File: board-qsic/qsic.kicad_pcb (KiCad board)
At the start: 4 copper layers, 214.1 x 131.7 mm, 173 parts, among them J101 Conn_02x05_Odd_Even, J102 Conn_02x07_Odd_Even, J301 SD Card, J302 SD Card, J501 USB_A, J601 QBUS_A, J602 QBUS_B, P501 Indicator Panel, U101 XC7A75T-CSG324, U1304 TPS82085, U1305 TPS82085, U1306 TPS82085, U1307 TPS82085, U301 IS43TR16128B, U501 MT25Q-mlq8, U502 TPS2561, U503 MAX3033E, U504 USB3340, U601 DS8641-small, U602 DS8641-small, U603 DS8641-small, U604 DS8641-small, U605 DS8641-small, U606 DS8641-small, U607 DS8641-small, U608 DS8641-small, U609 DS8641-small, U610 DS8641-small, U611 DS8641-small, U621 74LVC8T245-small, U622 74LVC8T245-small, U623 74LVC8T245-small, U624 74LVC8T245-small, U625 74LVC8T245-small, U626 74LVC8T245-small, U627 74LVC8T245-small, U628 74LVC8T245-small, U629 74LVC8T245-small, U630 74LVC8T245-small, U631 74LVC8T245-small, X501 ASE-24.000MHz

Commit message: Updated the date on all the pages.
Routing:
- net /QBUS & I/O/RPOK: track 55.1 -> 58.3 mm
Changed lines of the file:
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@@
     (thickness 1.6)
     (drawings 38)
-    (tracks 3850)
+    (tracks 3851)
     (zones 0)
     (modules 173)
@@
   (title_block
     (title QSIC)
-    (date 2019-10-10)
+    (date 2019-10-12)
     (rev 0.2)
   )
@@
   )
   (setup
-    (last_trace_width 0.127)
+    (last_trace_width 0.254)
     (user_trace_width 0.127)
     (user_trace_width 0.1524)
@@
     (visible_elements FFFFFF7F)
     (pcbplotparams
-      (layerselection 0x200f0_80000001)
+      (layerselection 0x200f0_ffffffff)
       (usegerberextensions false)
       (usegerberattributes false)
       (usegerberadvancedattributes false)
       (creategerberjobfile false)
-      (excludeedgelayer true)
+      (excludeedgelayer false)
       (linewidth 0.100000)
       (plotframeref false)
@@
   (segment (start 158.876999 94.487999) (end 158.75 94.361) (width 0.127) (layer F.Cu) (net 365))
   (via (at 159.258004 94.234) (size 0.254) (drill 0.2032) (layers F.Cu B.Cu) (net 366))
-  (segment (start 178.518 103.449) (end 168.473004 103.449) (width 0.127) (layer F.Cu) (net 366))
-  (segment (start 168.473004 103.449) (end 159.385003 94.360999) (width 0.127) (layer F.Cu) (net 366))
-  (segment (start 159.385003 94.360999) (end 159.258004 94.234) (width 0.127) (layer F.Cu) (net 366))
   (segment (start 134.01854 89.00146) (end 134.41708 89.4) (width 0.127) (layer F.Cu) (net 366))
   (segment (start 134.546999 89.273001) (end 134.42 89.4) (width 0.127) (layer B.Cu) (net 366))
@@
   (segment (start 156.337004 91.313) (end 139.573 91.313) (width 0.127) (layer B.Cu) (net 366))
   (segment (start 139.573 91.313) (end 137.336915 89.076915) (width 0.127) (layer B.Cu) (net 366))
+  (segment (start 159.385003 94.360999) (end 159.258004 94.234) (width 0.127) (layer F.Cu) (net 366))
+  (segment (start 178.518 103.449) (end 177.516 103.449) (width 0.127) (layer F.Cu) (net 366))
+  (segment (start 168.592506 103.568502) (end 159.385003 94.360999) (width 0.127) (layer F.Cu) (net 366))
+  (segment (start 177.396498 103.568502) (end 168.592506 103.568502) (width 0.127) (layer F.Cu) (net 366))
+  (segment (start 177.516 103.449) (end 177.396498 103.568502) (width 0.127) (layer F.Cu) (net 366))
   (via (at 134.42 86.2) (size 0.254) (drill 0.2032) (layers F.Cu B.Cu) (net 367))
   (segment (start 134.01854 85.80146) (end 134.02146 85.80146) (width 0.127) (layer F.Cu) (net 367) (status 30))
@@
   (segment (start 134.01854 85.00146) (end 134.02146 85.00146) (width 0.127) (layer F.Cu) (net 368) (status 30))
   (via (at 134.42 85.4) (size 0.254) (drill 0.2032) (layers F.Cu B.Cu) (net 368))
-  (via (at 176.82 102.8) (size 0.254) (drill 0.2032) (layers F.Cu B.Cu) (net 368))
-  (segment (start 178.518 102.799) (end 176.821 102.799) (width 0.127) (layer F.Cu) (net 368) (status 10))
-  (segment (start 176.821 102.799) (end 176.82 102.8) (width 0.127) (layer F.Cu) (net 368))
-  (segment (start 164.084 85.471) (end 154.94 85.471) (width 0.127) (layer B.Cu) (net 368))
   (segment (start 134.42 85.4) (end 134.82 85) (width 0.127) (layer Pwr.Cu) (net 368))
   (segment (start 140.282395 85.725) (end 140.462 85.725) (width 0.127) (layer Pwr.Cu) (net 368))
-  (segment (start 154.686 85.725) (end 140.641605 85.725) (width 0.127) (layer B.Cu) (net 368))
-  (segment (start 176.82 102.8) (end 171.958 97.938) (width 0.127) (layer B.Cu) (net 368))
   (segment (start 134.82 85) (end 136.42 85) (width 0.127) (layer Pwr.Cu) (net 368))
   (segment (start 137.145 85.725) (end 140.282395 85.725) (width 0.127) (layer Pwr.Cu) (net 368))
-  (segment (start 154.94 85.471) (end 154.686 85.725) (width 0.127) (layer B.Cu) (net 368))
   (segment (start 136.42 85) (end 137.145 85.725) (width 0.127) (layer Pwr.Cu) (net 368))
-  (segment (start 171.958 93.345) (end 164.084 85.471) (width 0.127) (layer B.Cu) (net 368))
-  (segment (start 171.958 97.938) (end 171.958 93.345) (width 0.127) (layer B.Cu) (net 368))
-  (segment (start 140.641605 85.725) (end 140.462 85.725) (width 0.127) (layer B.Cu) (net 368))
   (via (at 140.462 85.725) (size 0.254) (drill 0.2032) (layers F.Cu B.Cu) (net 368))
+  (segment (start 140.462 85.725) (end 154.686 85.725) (width 0.127) (layer B.Cu) (net 368))
+  (segment (start 171.322998 102.563395) (end 171.322998 102.743) (width 0.127) (layer B.Cu) (net 368))
+  (segment (start 154.94 85.471) (end 164.084 85.471) (width 0.127) (layer B.Cu) (net 368))
+  (segment (start 171.378998 102.799) (end 171.322998 102.743) (width 0.127) (layer F.Cu) (net 368))
+  (segment (start 164.084 85.471) (end 171.322998 92.709998) (width 0.127) (layer B.Cu) (net 368))
+  (segment (start 171.322998 92.709998) (end 171.322998 102.563395) (width 0.127) (layer B.Cu) (net 368))
+  (via (at 171.322998 102.743) (size 0.254) (drill 0.2032) (layers F.Cu B.Cu) (net 368))
+  (segment (start 178.518 102.799) (end 171.378998 102.799) (width 0.127) (layer F.Cu) (net 368))
+  (segment (start 154.686 85.725) (end 154.94 85.471) (width 0.127) (layer B.Cu) (net 368))
   (via (at 134.42 84.6) (size 0.254) (drill 0.2032) (layers F.Cu B.Cu) (net 369))
   (segment (start 134.01854 84.20146) (end 134.02146 84.20146) (width 0.127) (layer F.Cu) (net 369) (status 30))

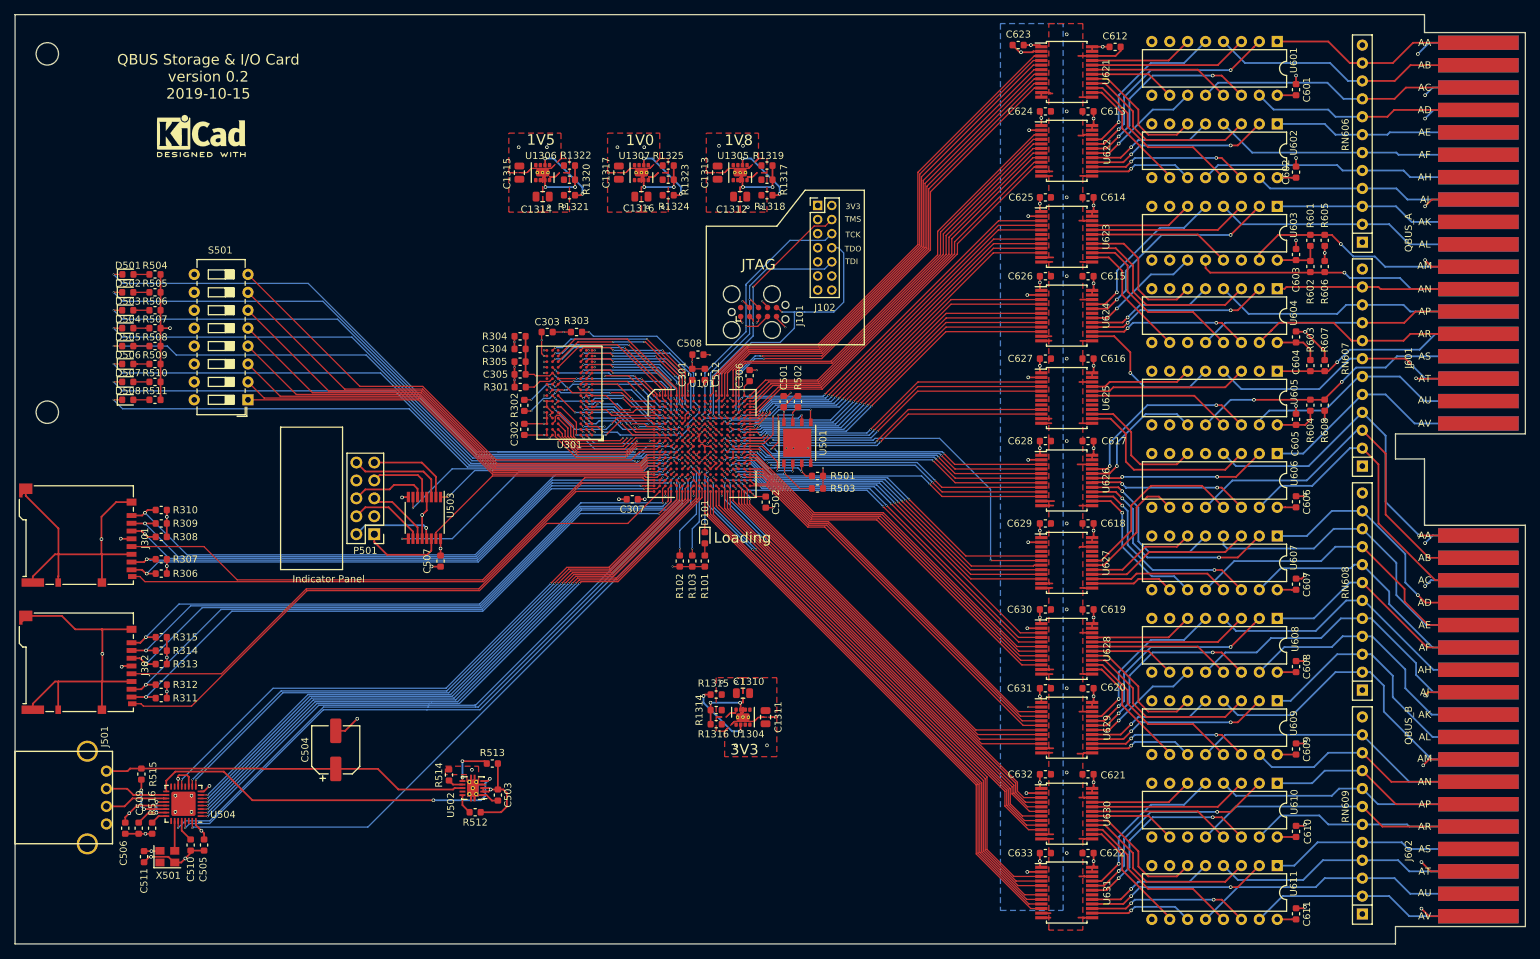
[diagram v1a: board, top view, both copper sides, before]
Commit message: Changes from Emanuel's comments.
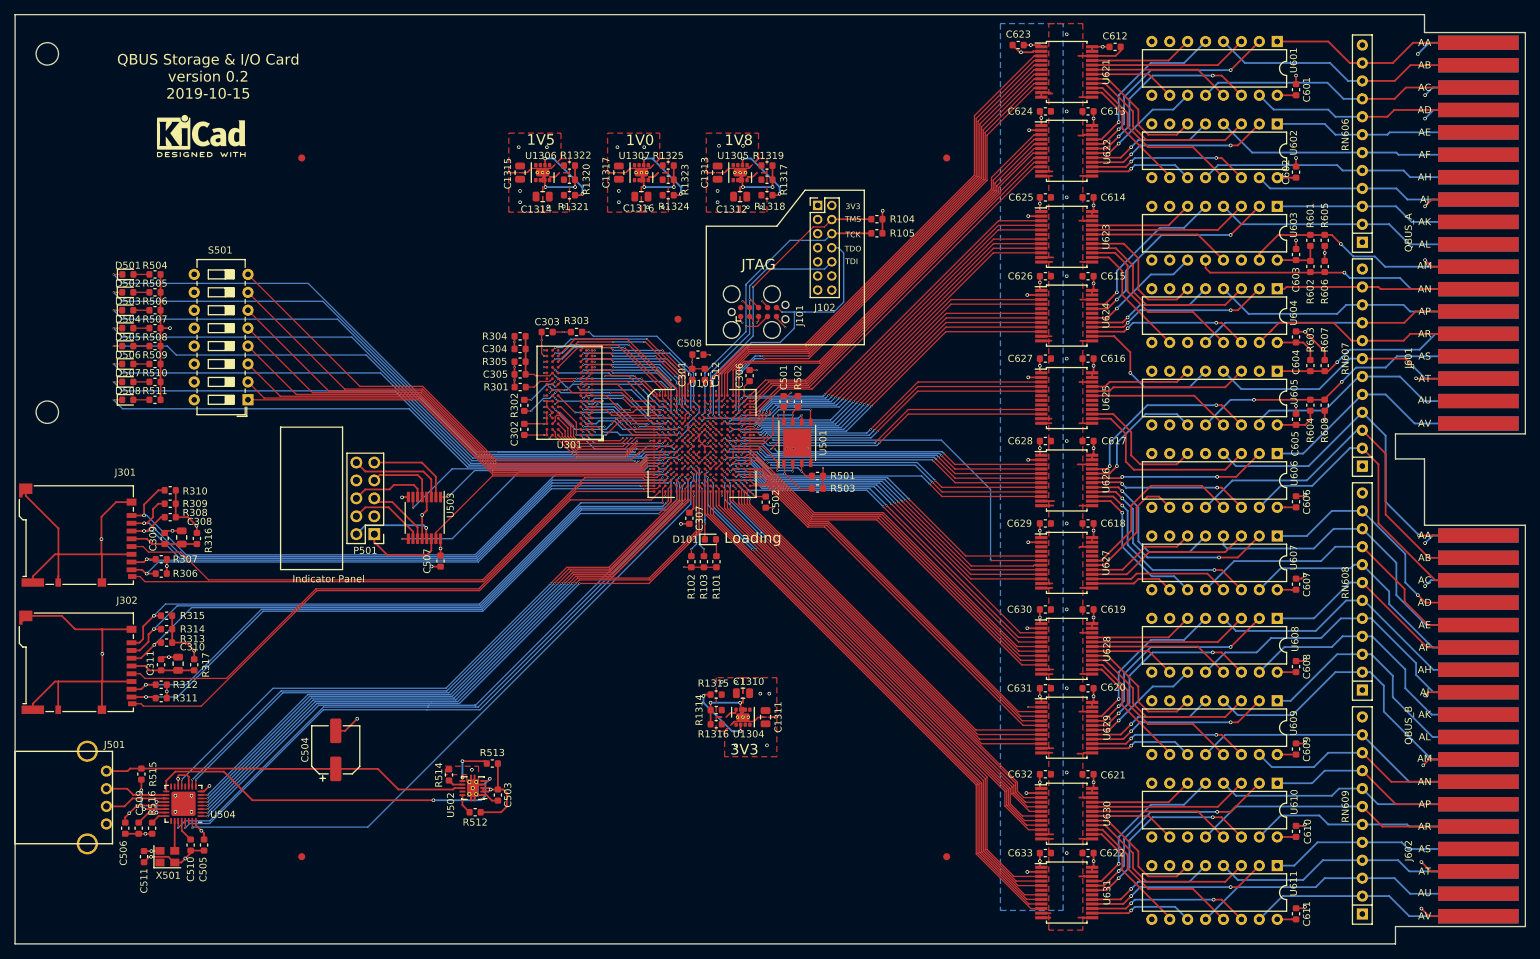
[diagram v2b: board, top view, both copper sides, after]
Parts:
- added C308: 22uF, Capacitor_SMD:C_0805_2012Metric, F.Cu at (56.6, 99.5)
- added C309: 100nF, Capacitor_SMD:C_0603_1608Metric, F.Cu at (54.2, 99.7)
- added C310: 22uF, Capacitor_SMD:C_0805_2012Metric, F.Cu at (56.1, 117.4)
- added C311: 100nF, Capacitor_SMD:C_0603_1608Metric, F.Cu at (53.7, 117.6)
- added FID101: Fiducial, Fiducial:Fiducial_1mm_Mask2mm, F.Cu at (73.7, 45.7)
- added FID102: Fiducial, Fiducial:Fiducial_1mm_Mask2mm, F.Cu at (165.1, 45.7)
- added FID103: Fiducial, Fiducial:Fiducial_1mm_Mask2mm, F.Cu at (73.7, 144.8)
- added FID104: Fiducial, Fiducial:Fiducial_1mm_Mask2mm, F.Cu at (165.1, 144.8)
- added FID105: Fiducial, Fiducial:Fiducial_1mm_Mask2mm, F.Cu at (127.0, 68.6)
- added R104: 10k, Resistor_SMD:R_0603_1608Metric, F.Cu at (155.2, 54.4)
- added R105: 10k, Resistor_SMD:R_0603_1608Metric, F.Cu at (155.2, 56.4)
- added R316: 4.7, Resistor_SMD:R_0603_1608Metric, F.Cu at (58.8, 99.7)
- added R317: 4.7, Resistor_SMD:R_0603_1608Metric, F.Cu at (58.4, 117.6)
- R304, R305: value 47 -> 47 1%
- moved C307 8.53 mm to (128.6, 96.8), turned to 270 degrees
- moved R315 3.14 mm to (54.5, 110.6)
- moved R313 3.14 mm to (54.5, 114.4)
- moved R314 3.14 mm to (54.5, 112.5)
- moved R308 3.07 mm to (55.0, 96.6)
- moved R310 3.07 mm to (55.0, 92.8)
- moved R309 3.07 mm to (55.0, 94.7)
- moved R101 1.65 mm to (132.5, 103.0)
- moved R103 1.65 mm to (130.7, 103.0)
- moved R102 1.65 mm to (128.9, 103.0)
- moved D101 0.83 mm to (131.6, 99.8), turned to 0 degrees
- moved C1315 0.10 mm to (104.6, 47.8)
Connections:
- J301 pad 4: /3V3 -> Net-(C308-Pad1)
- J302 pad 4: /3V3 -> Net-(C310-Pad1)
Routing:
- net /3V3: track 125.3 -> 136.5 mm, vias 56 -> 54
- net Net-(C308-Pad1): track 0.00 -> 9.57 mm
- net Net-(C310-Pad1): track 0.00 -> 9.14 mm
- net /TMS: track 37.3 -> 42.9 mm
- net /TCK: track 40.5 -> 46.1 mm
- net GND: track 382.5 -> 387.7 mm, vias 126 -> 136
- net /QBUS & I/O/sd0_dat2: track 85.8 -> 89.1 mm
- net /QBUS & I/O/sd0_dat3: track 84.8 -> 88.0 mm
- net /QBUS & I/O/usb0_d1: track 91.0 -> 93.8 mm
- net /QBUS & I/O/usb0_d0: track 89.9 -> 92.6 mm
- net /QBUS & I/O/usb0_nxt: track 91.4 -> 94.2 mm
- net /QBUS & I/O/sd0_cmd: track 84.4 -> 86.4 mm
- net /QBUS & I/O/RDAL17: track 72.3 -> 71.1 mm
- net /QBUS & I/O/TDOUT: track 58.0 -> 56.8 mm
- net /QBUS & I/O/RIRQ5: track 74.0 -> 72.9 mm
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
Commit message: Changed some capacitors from 100nF to 10uF
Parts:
- C301, C306, C307, C502, C508, C512: value 100nF -> 10uF
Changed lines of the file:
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@@
       (effects (font (size 1 1) (thickness 0.15)))
     )
-    (fp_text value 100nF (at 0 1.43 90) (layer F.Fab)
+    (fp_text value 10uF (at 0 1.43 90) (layer F.Fab)
       (effects (font (size 1 1) (thickness 0.15)))
     )
@@
       (effects (font (size 1 1) (thickness 0.15)))
     )
-    (fp_text value 100nF (at 0 1.43) (layer F.Fab)
+    (fp_text value 10uF (at 0 1.43) (layer F.Fab)
       (effects (font (size 1 1) (thickness 0.15)))
     )
@@
       (effects (font (size 1 1) (thickness 0.15)))
     )
-    (fp_text value 100nF (at 0 1.43 90) (layer F.Fab)
+    (fp_text value 10uF (at 0 1.43 90) (layer F.Fab)
       (effects (font (size 1 1) (thickness 0.15)))
     )
@@
       (effects (font (size 1 1) (thickness 0.15)))
     )
-    (fp_text value 100nF (at 0 1.43 90) (layer F.Fab)
+    (fp_text value 10uF (at 0 1.43 90) (layer F.Fab)
       (effects (font (size 1 1) (thickness 0.15)))
     )
@@
       (effects (font (size 1 1) (thickness 0.15)))
     )
-    (fp_text value 100nF (at 0 1.43 90) (layer F.Fab)
+    (fp_text value 10uF (at 0 1.43 90) (layer F.Fab)
       (effects (font (size 1 1) (thickness 0.15)))
     )
@@
       (effects (font (size 1 1) (thickness 0.15)))
     )
-    (fp_text value 100nF (at 0 1.43 90) (layer F.Fab)
+    (fp_text value 10uF (at 0 1.43 90) (layer F.Fab)
       (effects (font (size 1 1) (thickness 0.15)))
     )

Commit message: These are all old changes in directories that are now historical.
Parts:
- C1310, C1312, C1314, C1316, C308, C310: value 22uF -> 22µF
- C1311, C1313, C1315, C1317, C301, C306, C508, C512: value 10uF -> 10µF
- C504: value 150uF -> 150µF
- C509, C510: value 1uF -> 1µF
- J301: value SD Card -> SD 0
- J302: value SD Card -> SD 1
- moved J602 0.07 mm to (234.3, 98.2)
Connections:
- U504 pad 18: Net-(J501-Pad2) -> Net-(J501-Pad3)
- U504 pad 19: Net-(J501-Pad3) -> Net-(J501-Pad2)
